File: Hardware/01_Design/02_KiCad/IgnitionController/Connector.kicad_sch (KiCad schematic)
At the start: 0 parts

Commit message: Updates to HW Layout
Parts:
- added J1: 770669-1, 7706691:7706691, symbol 770669-1:770669-1
- added J2: Conn_02x03_Odd_Even, Connector_IDC:IDC-Header_2x03_P2.54mm_Vertical, symbol Connector_Generic:Conn_02x03_Odd_Even
- added J3: FTSH-105-01-L-DV-A, FTSH-105-01-L-DV-A:FTSH-105-XX-YYY-DV-A, symbol FTSH-105-01-L-DV-A:FTSH-105-01-L-DV-A
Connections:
- new net +BATT: J1.2
- new net CAN-H: J1.5
- new net CAN-L: J1.17
- new net COOLANT_TEMP_SIGNAL: J1.13
- new net GND: J1.1, J1.15, J1.19, J2.6 (Pin_6), J3.3, J3.5
- new net IGN_COIL_1: J1.7
- new net IGN_COIL_2: J1.20
- new net IGN_COIL_3: J1.8
- new net IGN_COIL_4: J1.21
- new net INJ_FUEL_1: J1.9
- new net INJ_FUEL_2: J1.22
- new net INJ_FUEL_3: J1.10
- new net INJ_FUEL_4: J1.23
- new net KL15: J1.3
- new net MAP_SENSOR_SIGNAL: J1.11
- new net MCU_NRST: J3.10
- new net PMIC_RESET: J2.5 (Pin_5)
- new net PMIC_SPI_MISO: J2.1 (Pin_1)
- new net PMIC_SPI_MOSI: J2.4 (Pin_4)
- new net PMIC_SPI_SCK: J2.3 (Pin_3)
- new net SENSOR_1_SIGNAL: J1.4
- new net SENSOR_2_SIGNAL: J1.16
- new net SWCLK_Pin: J3.4
- new net SWDIO_Pin: J3.2
- new net TPS_SIGNAL: J1.12
- new net UART_RX: J1.6
- new net UART_TX: J1.18
- new net VMCU_OUT: J3.1
- new net VPMIC: J2.2 (Pin_2)
- new net VSEN: J1.14
- no-connect marks 0 -> 4
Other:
- note added: "MAIN CONNECTOR"
- note added: "MCU CONNECTOR"
- note added: "PMIC CONNECTOR"

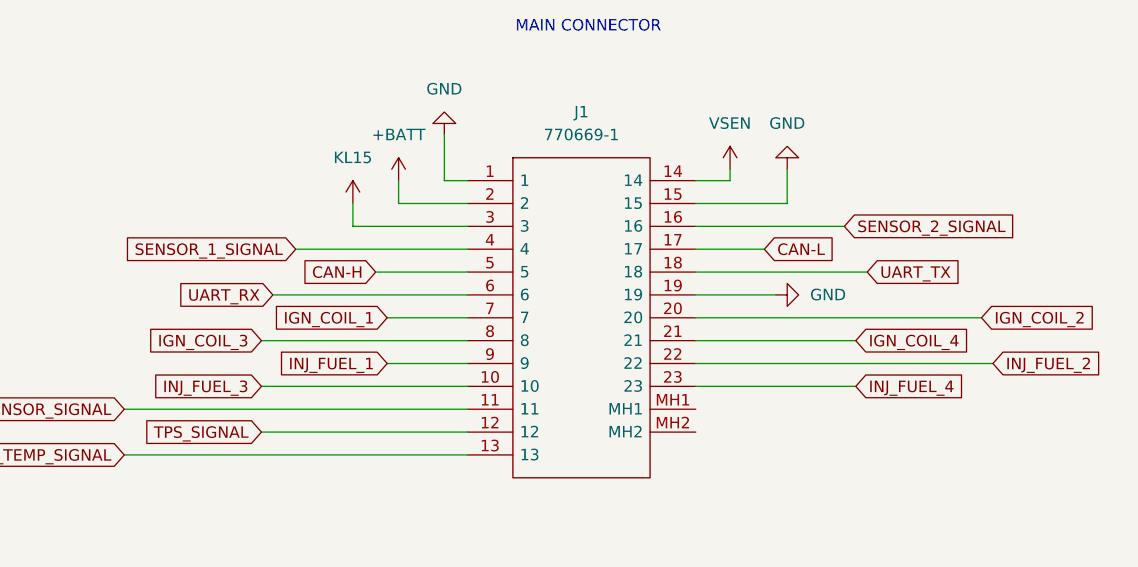
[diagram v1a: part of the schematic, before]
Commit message: Updated Solder Mask labels
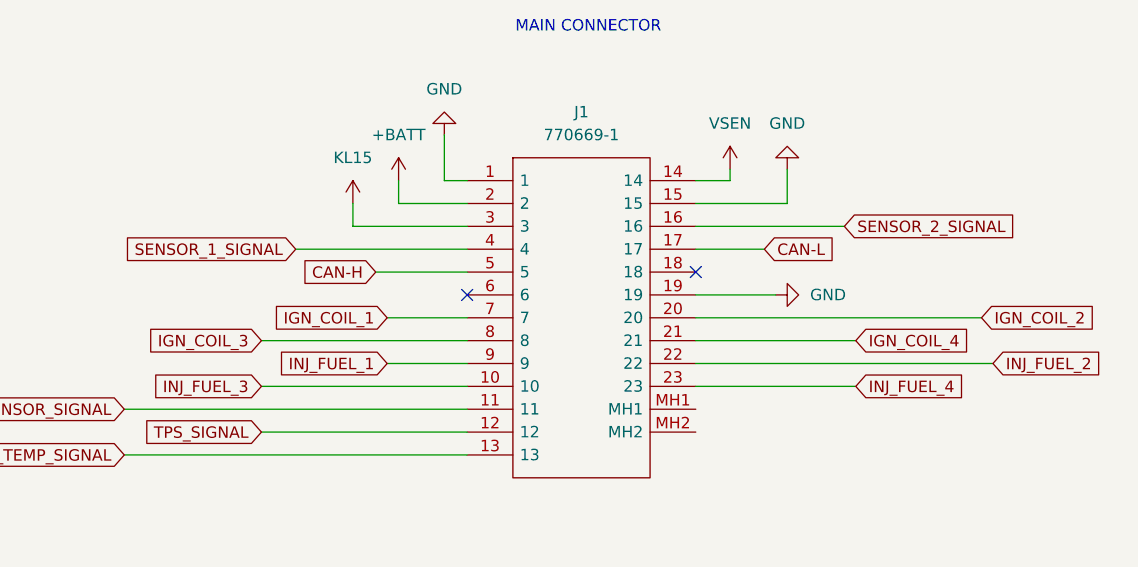
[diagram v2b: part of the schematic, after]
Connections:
- net UART_RX: no longer names the net of J1.6
- net UART_TX: no longer names the net of J1.18
- no-connect marks 4 -> 6
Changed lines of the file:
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@@
+	)
+	(no_connect
+		(at 101.6 53.34)
+	)
+	(no_connect
+		(at 127 50.8)
 	)
 	(no_connect
@@
 	(wire
 		(pts
-			(xy 127 50.8) (xy 146.05 50.8)
-		)
-		(stroke
-			(width 0)
-			(type default)
-		)
-	)
-	(wire
-		(pts
 			(xy 88.9 45.72) (xy 101.6 45.72)
 		)
@@
 		(pts
 			(xy 93.98 40.64) (xy 93.98 43.18)
-		)
-		(stroke
-			(width 0)
-			(type default)
-		)
-	)
-	(wire
-		(pts
-			(xy 80.01 53.34) (xy 101.6 53.34)
 		)
 		(stroke
@@
 		)
 	)
-	(global_label "UART_TX"
-		(shape input)
-		(at 146.05 50.8 0)
-		(fields_autoplaced yes)
-		(effects
-			(font
-				(size 1.27 1.27)
-			)
-			(justify left)
-		)
-		(property "Intersheetrefs" "${INTERSHEET_REFS}"
-			(at 156.8366 50.8 0)
-			(effects
-				(font
-					(size 1.27 1.27)
-				)
-				(justify left)
-				(hide yes)
-			)
-		)
-	)
 	(global_label "INJ_FUEL_2"
 		(shape input)
@@
 				(hide yes)
 			)
-		)
-	)
-	(global_label "UART_RX"
-		(shape input)
-		(at 80.01 53.34 180)
-		(fields_autoplaced yes)
-		(effects
-			(font
-				(size 1.27 1.27)
-			)
-			(justify right)
-		)
-		(property "Intersheetrefs" "${INTERSHEET_REFS}"
-			(at 68.921 53.34 0)
-			(effects
-				(font
-					(size 1.27 1.27)
-				)
-				(justify right)
-				(hide yes)
-			)
